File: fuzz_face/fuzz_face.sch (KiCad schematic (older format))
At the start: 15 parts, among them Q1 Q_PNP_EBC, Q2 Q_PNP_EBC

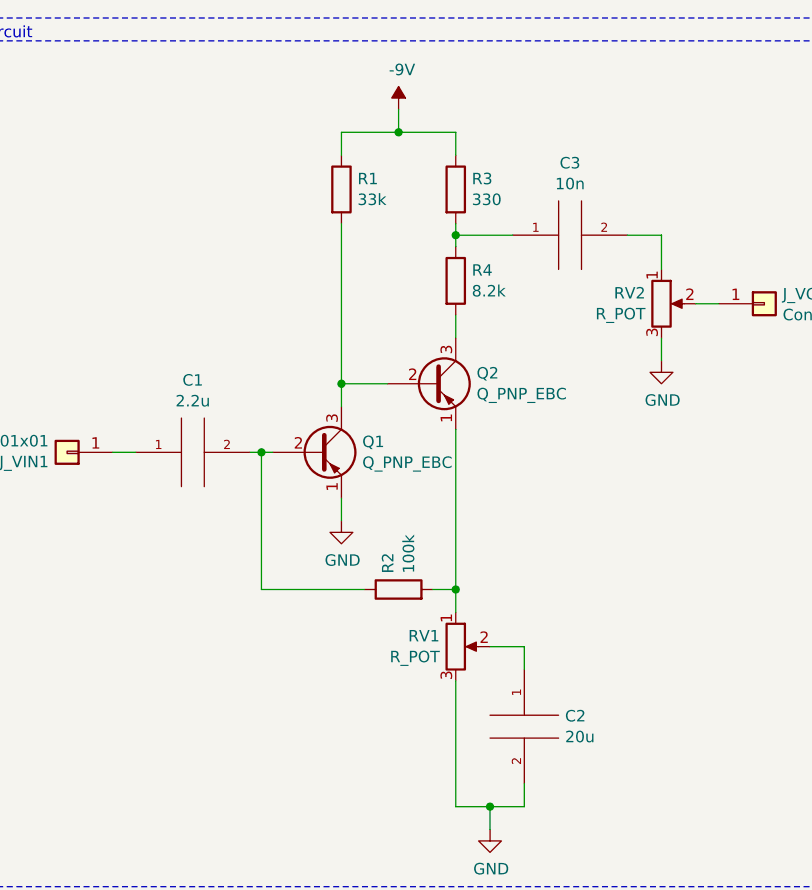
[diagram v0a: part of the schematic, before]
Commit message: Add simple common drain buffer.
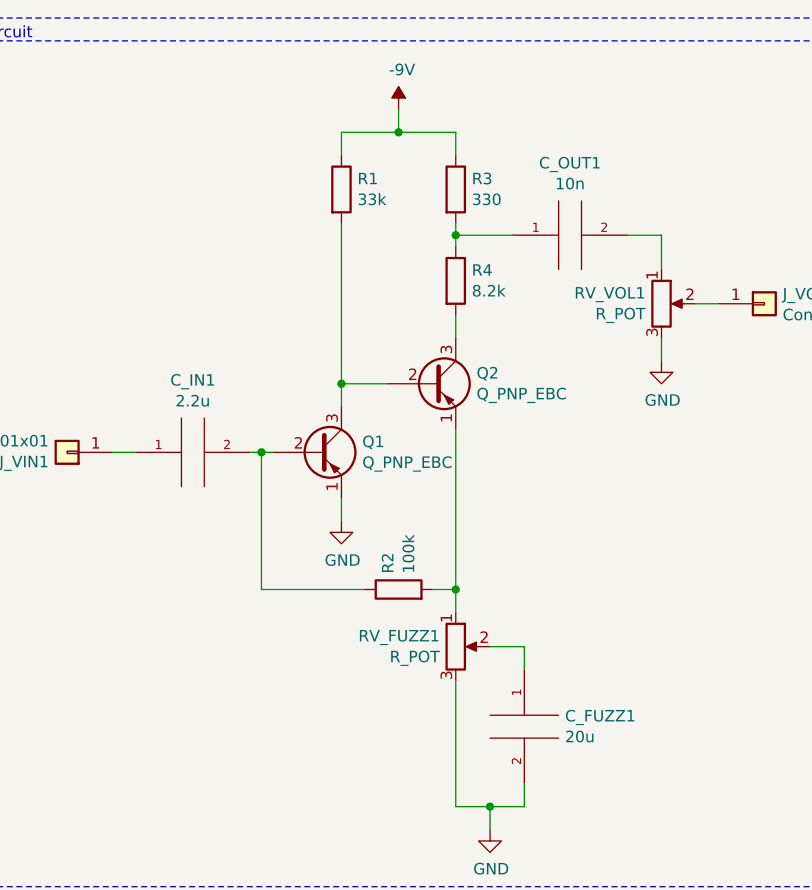
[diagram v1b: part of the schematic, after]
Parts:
- renumbered C2 to C_FUZZ1, C1 to C_IN1, C3 to C_OUT1, RV1 to RV_FUZZ1, RV2 to RV_VOL1
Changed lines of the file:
@@
 Dec 23, 2018\n
 $Comp
-L pspice:C C1
+L pspice:C C_IN1
 U 1 1 5C1F4DD3
 P 4050 2550
-F 0 "C1" V 4365 2550 50  0000 C CNN
+F 0 "C_IN1" V 4365 2550 50  0000 C CNN
 F 1 "2.2u" V 4274 2550 50  0000 C CNN
 F 2 "Capacitor_THT:C_Disc_D9.0mm_W5.0mm_P10.00mm" H 4050 2550 50  0001 C CNN
@@
 $EndComp
 $Comp
-L pspice:C C3
+L pspice:C C_OUT1
 U 1 1 5C1F4E3A
 P 5700 1600
-F 0 "C3" V 6015 1600 50  0000 C CNN
+F 0 "C_OUT1" V 6015 1600 50  0000 C CNN
 F 1 "10n" V 5924 1600 50  0000 C CNN
 F 2 "Capacitor_THT:C_Disc_D9.0mm_W5.0mm_P10.00mm" H 5700 1600 50  0001 C CNN
@@
 $EndComp
 $Comp
-L Device:R_POT RV2
+L Device:R_POT RV_VOL1
 U 1 1 5C1F5EC0
 P 6100 1900
-F 0 "RV2" H 6030 1946 50  0000 R CNN
+F 0 "RV_VOL1" H 6030 1946 50  0000 R CNN
 F 1 "R_POT" H 6030 1855 50  0000 R CNN
 F 2 "TerminalBlock:TerminalBlock_bornier-3_P5.08mm" H 6100 1900 50  0001 C CNN
@@
 $EndComp
 $Comp
-L Device:R_POT RV1
+L Device:R_POT RV_FUZZ1
 U 1 1 5C1F5FAC
 P 5200 3400
-F 0 "RV1" H 5130 3446 50  0000 R CNN
+F 0 "RV_FUZZ1" H 5130 3446 50  0000 R CNN
 F 1 "R_POT" H 5130 3355 50  0000 R CNN
 F 2 "TerminalBlock:TerminalBlock_bornier-3_P5.08mm" H 5200 3400 50  0001 C CNN
@@
 $EndComp
 $Comp
-L pspice:C C2
+L pspice:C C_FUZZ1
 U 1 1 5C1FCAA2
 P 5500 3750
-F 0 "C2" H 5678 3796 50  0000 L CNN
+F 0 "C_FUZZ1" H 5678 3796 50  0000 L CNN
 F 1 "20u" H 5678 3705 50  0000 L CNN
 F 2 "Capacitor_THT:C_Disc_D9.0mm_W5.0mm_P10.00mm" H 5500 3750 50  0001 C CNN
@@
 	650  1650 2800 1650
 $Comp
-L power:-9V #PWR?
+L power:-9V #PWR07
 U 1 1 5C2B33B3
 P 2350 1000
-F 0 "#PWR?" H 2350 875 50  0001 C CNN
+F 0 "#PWR07" H 2350 875 50  0001 C CNN
 F 1 "-9V" H 2365 1173 50  0000 C CNN
 F 2 "" H 2350 1000 50  0001 C CNN
